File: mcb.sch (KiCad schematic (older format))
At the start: 11 parts

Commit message: more voice work
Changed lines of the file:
@@
 	2775 3600 2350 3600
 Connection ~ 2350 3600
-Wire Notes Line
-	700  1700 7925 1700
-Wire Notes Line
-	7925 1700 7925 4750
-Wire Notes Line
-	7925 4750 700  4750
-Wire Notes Line
-	700  4750 700  1700
 $EndSCHEMATC

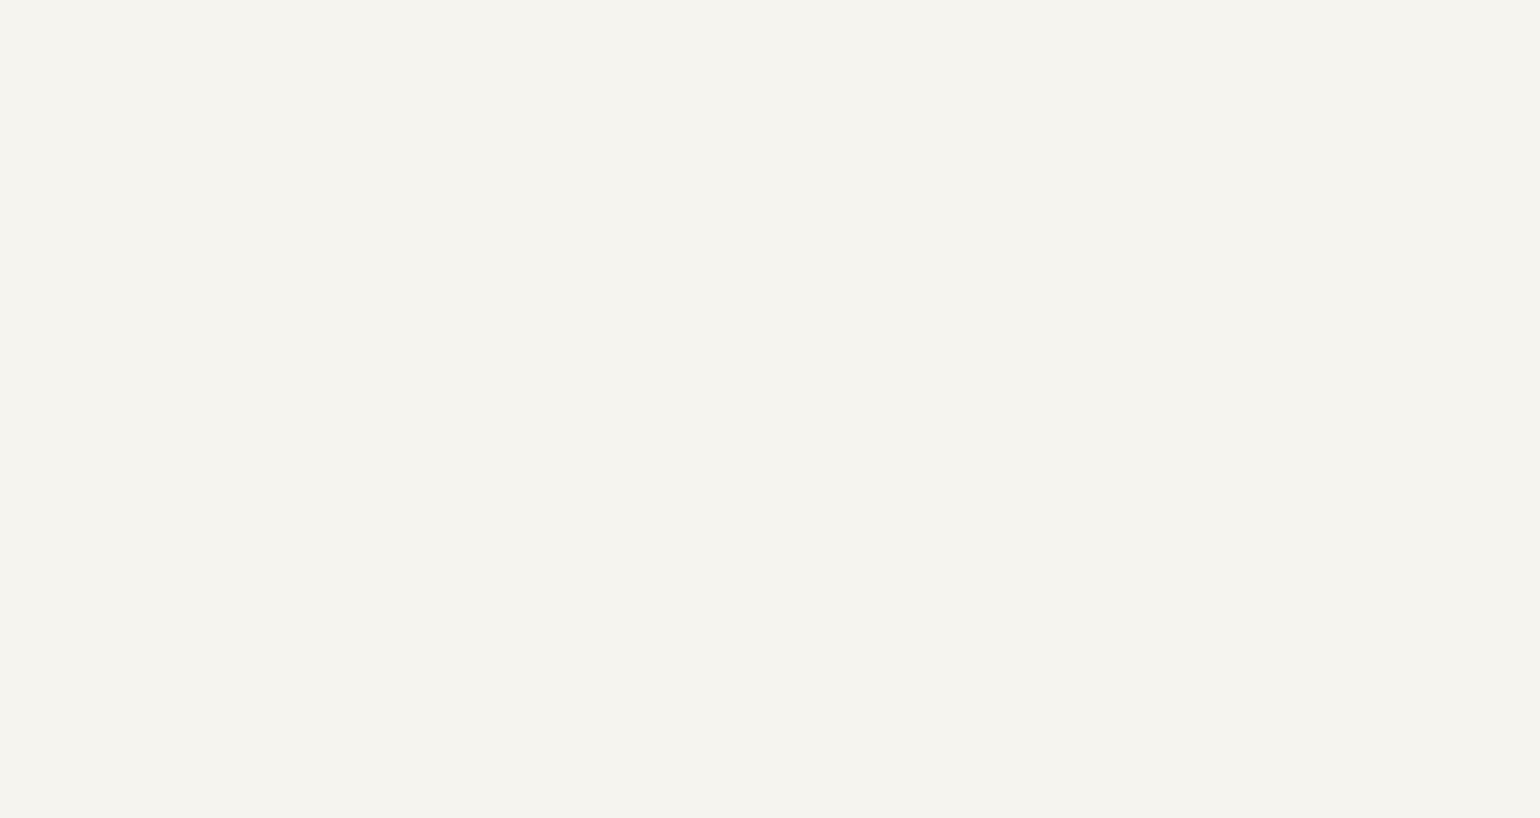
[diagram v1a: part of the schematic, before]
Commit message: added DDR3 240 connector, starting to connect input and output labels
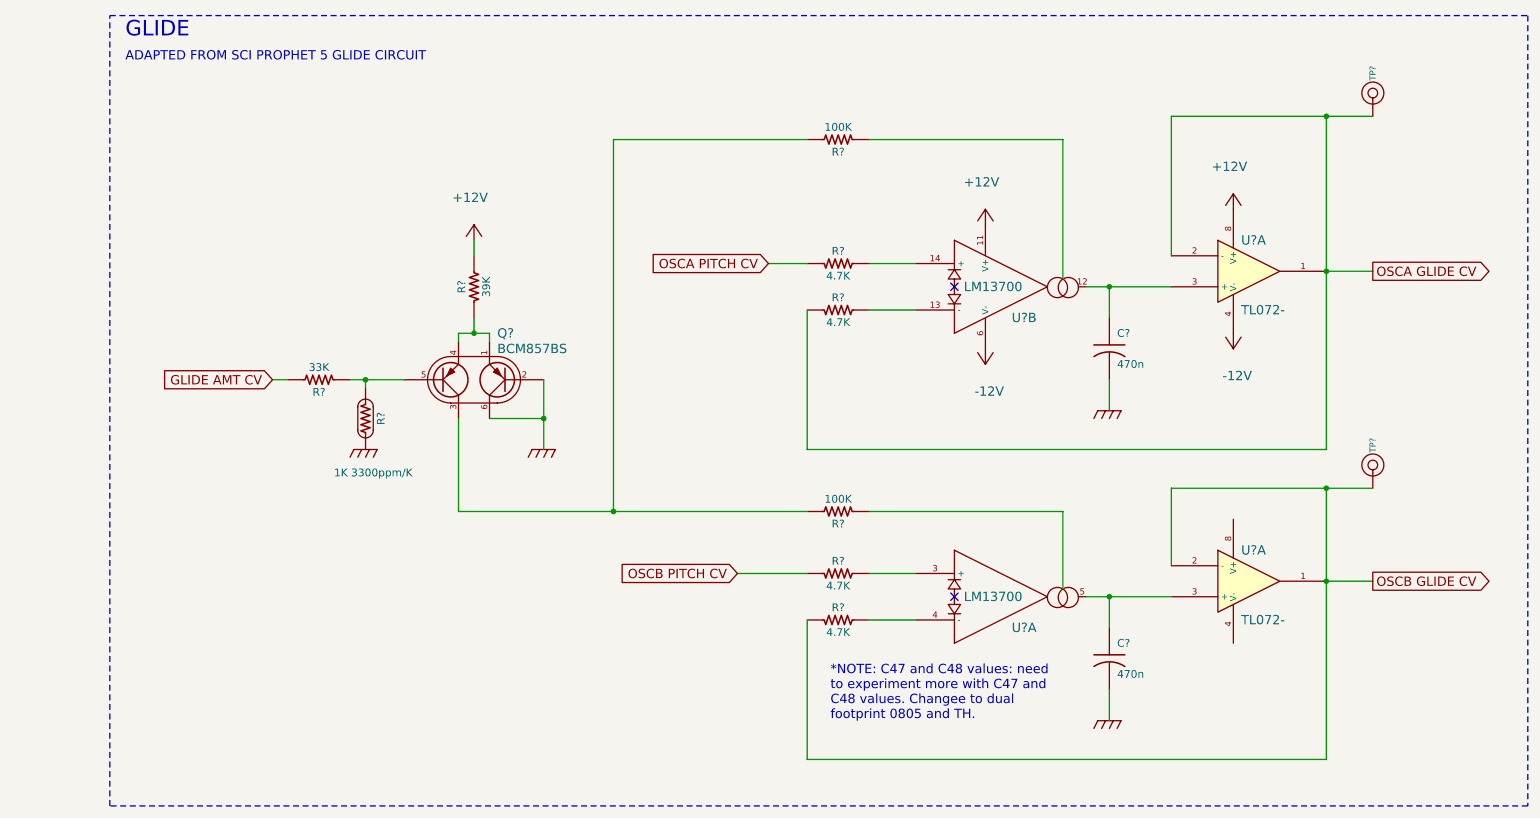
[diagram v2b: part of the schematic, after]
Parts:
- added C? (x2): 470n, ~, symbol C_US
- added Q?: BCM857BS, ~, symbol BCM857BS
- added R? (x4): 4.7K, ~, symbol R_US
- added R? (x2): 100K, symbol R_US
- added R?: 39K, ~, symbol R_US
- added R?: 33K, symbol R_US
- added R?: 1K 3300ppm/K, ~, symbol R_TEMPCO
- added TP? (x2): CONN_1, ~, symbol CONN_1
- added U? (x2): LM13700, ~, symbol LM13700
- added U? (x2): TL072-, ~, symbol TL072-
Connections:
- net +12V: now also R?.2, U?.11 (V+), U?.8 (V+)
- net -12V: now also U?.4 (V-), U?.6 (V-)
- net GND: now also C?.2, C?.2, Q?.2 (B1), Q?.6 (C1), R?.2
- new net: R?.2, U?.14 (+)
- new net: C?.1, U?.12, U?.3 (+)
- new net: R?.2, U?.13 (-)
- new net: R?.1, U?.16
- new net: R?.2, U?.3 (+)
- new net: R?.1, U?.1
- new net: R?.2, U?.4 (-)
- new net: C?.1, U?.3 (+), U?.5
- new net: Q?.1 (E1), Q?.4 (E2), R?.1
- new net: Q?.3 (C2), R?.2, R?.2
- new net: Q?.5 (B2), R?.1, R?.1
- new net GLIDE AMT CV: R?.2
- new net OSCA GLIDE CV: R?.1, TP?.1, U?.1, U?.2 (-)
- new net OSCA PITCH CV: R?.1
- new net OSCB GLIDE CV: R?.1, TP?.1, U?.1, U?.2 (-)
- new net OSCB PITCH CV: R?.1
- no-connect marks 0 -> 2
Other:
- note added: "*NOTE: C47 and C48 values: need\nto experiment more with C47 and \nC48 values. Changee to dual\nfootprint 0805 and TH."
- note added: "ADAPTED FROM SCI PROPHET 5 GLIDE CIRCUIT"
- note added: "GLIDE\n"
